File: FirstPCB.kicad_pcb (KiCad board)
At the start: 2 copper layers, 77.6 x 38.2 mm, 24 parts, among them SW1 SW_Push, U1 ATmega32U4-AU, Y1 16MHz

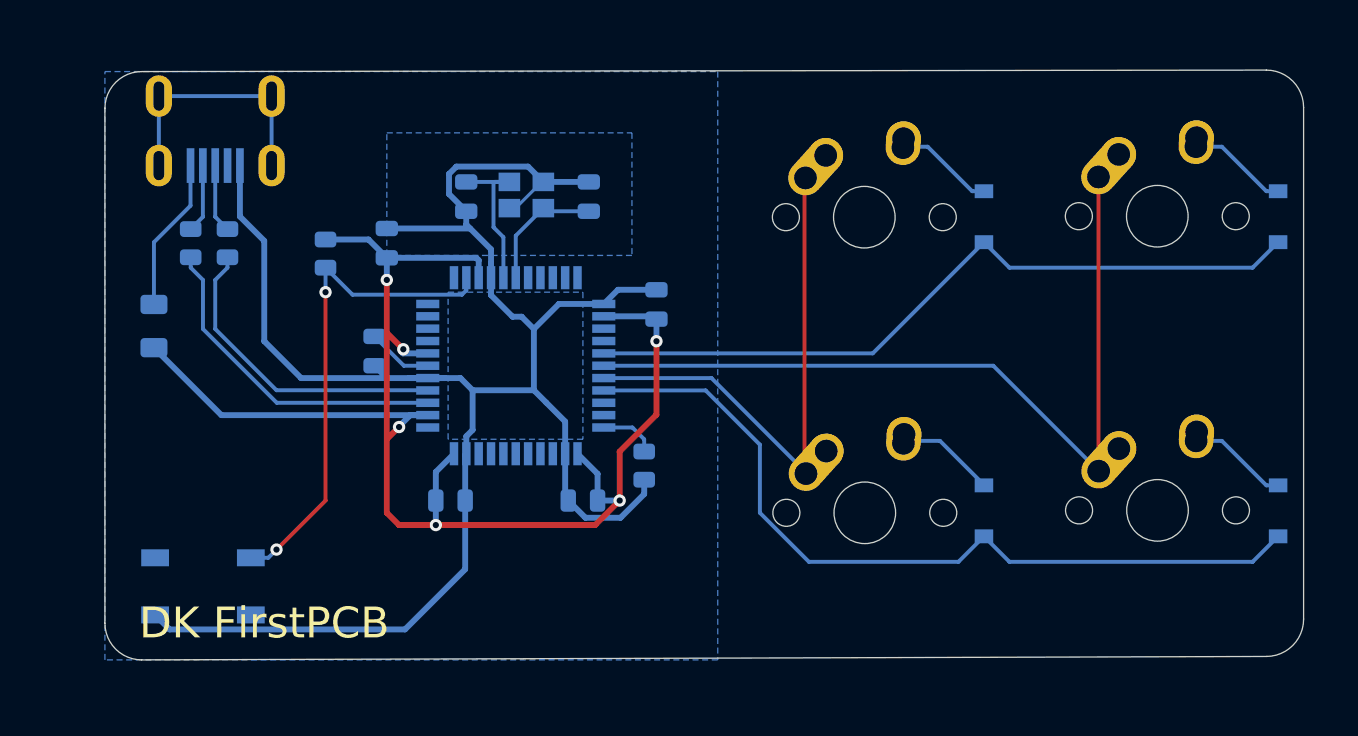
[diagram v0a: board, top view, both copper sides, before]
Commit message: Converted to USB Type-C
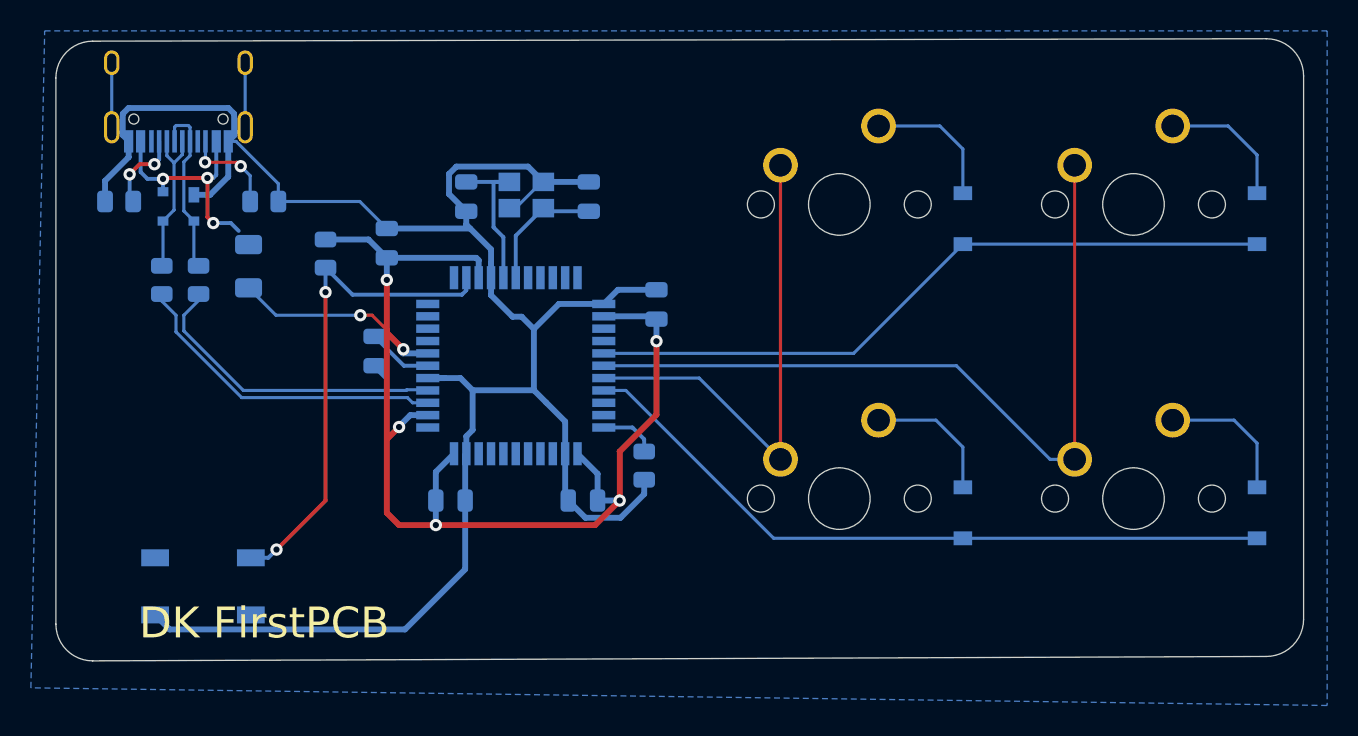
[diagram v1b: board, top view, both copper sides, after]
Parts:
- removed R2, R3: 22, Resistor_SMD:R_0805_2012Metric
- added R5: 22, Resistor_SMD:R_0805_2012Metric, B.Cu at (72.7, 120.7)
- added R6: 22, Resistor_SMD:R_0805_2012Metric, B.Cu at (75.1, 120.7)
- added R7: 5.1k, Resistor_SMD:R_0805_2012Metric, B.Cu at (70.0, 115.6)
- added R8: 5.1k, Resistor_SMD:R_0805_2012Metric, B.Cu at (79.4, 115.6)
- added U2: PRTR5V0U2X, locallib:SOT143B, B.Cu at (73.8, 115.9)
- MX1, MX2, MX3, MX4: footprint MX_Alps_Hybrid:MX-1U-NoLED -> MX_Only:MXOnly-1U-NoLED
- USB1: value Molex-0548190589 -> HRO-TYPE-C-31-M-12; footprint random-keyboard-parts:Molex-0548190589 -> Type-C:HRO-TYPE-C-31-M-12-Assembly
- moved F1 7.25 mm to (78.4, 119.8)
- moved USB1 5.32 mm to (73.8, 104.0), turned to 0 degrees
- moved MX3 1.89 mm to (116.6, 134.8)
- moved MX1 1.82 mm to (116.6, 115.8)
- moved MX4 1.73 mm to (135.7, 134.8)
- moved MX2 1.72 mm to (135.7, 115.8)
- moved D2 1.37 mm to (143.7, 116.7)
- moved D4 1.37 mm to (143.7, 135.7)
- moved D1 1.37 mm to (124.6, 116.7)
- moved D3 1.37 mm to (124.6, 135.7)
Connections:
- U1 pad 3: Net-(R3-Pad1) -> D-
- U1 pad 4: Net-(R2-Pad1) -> D+
- USB1 pad 2: Net-(USB1-Pad2) -> VCC
- USB1 pad 3: D+ -> Net-(USB1-Pad3)
- USB1 pad 4: D- -> Net-(R7-Pad2)
- USB1 pad 5: VCC -> Net-(R5-Pad2)
- USB1 pad 6: Net-(USB1-Pad6) -> Net-(R6-Pad2)
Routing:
- net Net-(R3-Pad1): track 21.5 -> 0.00 mm
- net GND: track 126.9 -> 148.0 mm
- net Net-(R2-Pad1): track 20.4 -> 0.00 mm
- net D-: track 4.10 -> 21.0 mm
- net Net-(USB1-Pad6): track 16.3 -> 0.00 mm
- net D+: track 4.09 -> 20.2 mm
- net Net-(R6-Pad2): track 0.00 -> 11.6 mm
- net Net-(R5-Pad2): track 0.00 -> 10.2 mm
- net +5V: track 96.8 -> 87.4 mm, vias 6 -> 7
- net ROW1: track 52.9 -> 46.3 mm
- net Net-(R8-Pad2): track 0.00 -> 6.32 mm, vias 0 -> 2
- net VCC: track 9.63 -> 15.1 mm, vias 0 -> 3
- net Net-(R7-Pad2): track 0.00 -> 5.34 mm, vias 0 -> 2
- net ROW0: track 48.0 -> 45.2 mm
- net Net-(D1-Pad2): track 6.50 -> 8.94 mm
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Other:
- board size 77.6 x 38.2 mm -> 80.8 x 40.3 mm
